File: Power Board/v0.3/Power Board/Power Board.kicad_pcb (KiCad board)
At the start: 2 copper layers, 66 x 80 mm, 72 parts, among them J1 Battery In, J2 JST B2PS-VH, J3 JST B2PS-VH, J4 JST B2PS-VH, J5 JST B2PS-VH, J6 JST B2PS-VH, J7 JST B2PS-VH, J8 Molex 70553-0006, Q1 SI5504BDC, SW1 SW_Push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

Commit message: Work in progress.
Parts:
- J1: footprint Power_Board:Molex_Microfit_43650-0203 -> Connector_JST:JST_VH_B3PS-VH_1x03_P3.96mm_Horizontal
- moved D1 32.0 mm to (124.0, 36.5)
- moved D2 32.0 mm to (130.2, 36.5)
- moved R1 32.0 mm to (124.0, 39.5)
- moved R2 32.0 mm to (130.1, 39.5)
- moved C5 27.0 mm to (99.0, 93.1)
- moved D3 27.0 mm to (94.0, 97.0)
- moved R5 27.0 mm to (97.0, 93.0)
- moved R6 27.0 mm to (97.0, 97.2)
- moved R7 27.0 mm to (99.0, 97.2)
- moved J1 21.6 mm to (105.0, 50.0), turned to 180 degrees
- moved C8 10.0 mm to (104.2, 80.0), turned to 180 degrees
- moved C10 9.19 mm to (107.2, 84.0)
- moved R12 9.06 mm to (100.0, 77.0)
- moved R8 9.06 mm to (100.0, 69.2)
- moved C2 9.00 mm to (99.8, 61.0)
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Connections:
- net Net-(C16-Pad1) renamed /Panel Power/Switch_Node
- net Net-(R18-Pad1) renamed /Panel Power/Drive_High_2
- net Net-(R18-Pad2) renamed /Panel Power/Drive_High_1
- net Net-(U2-Pad10) renamed /Panel Power/Drive_Low
- J1 pad 2: GND -> Net-(J1-Pad2)
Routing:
- net /5.2V_switched: track 0.00 -> 109.3 mm, vias 0 -> 2
- net /Pi Power/Power_Button: track 0.00 -> 72.0 mm
- net /Battery_Power: track 0.00 -> 69.8 mm
- net Net-(C5-Pad1): track 0.00 -> 39.6 mm, vias 0 -> 2
- net /Panel_Alert: track 0.00 -> 31.7 mm
- net /SCL: track 0.00 -> 23.7 mm
- net /Panel_Power: track 0.00 -> 21.5 mm, vias 0 -> 1
- net /SDA: track 0.00 -> 20.7 mm
- net Net-(C1-Pad1): track 0.00 -> 18.2 mm
- net /Panel Power/Vreg: track 0.00 -> 14.5 mm, vias 0 -> 2
- net Net-(C15-Pad1): track 0.00 -> 12.6 mm
- net Net-(C8-Pad2): track 0.00 -> 10.8 mm
- net Net-(R20-Pad2): track 0.00 -> 9.85 mm
- net Net-(R17-Pad2): track 0.00 -> 8.63 mm
- net Net-(R8-Pad2): track 0.00 -> 8.04 mm
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- added copper zone on F.Cu, net /5.2V_switched
- added copper zone on F.Cu, net /Battery_Power
- added copper zone on F.Cu, net /Panel Power/Switch_Node
- added copper zone on B.Cu, net /Panel_Power
- added copper zone on F.Cu, net /Panel_Power
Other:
- net class Panel_Battery added: clearance 0.1524, trace_width 3, via_dia 1, via_drill 0.5
- net class Panel_Drive added: clearance 0.1524, trace_width 0.25, via_dia 0.508, via_drill 0.254
- net class Pi_Battery added: clearance 0.1524, trace_width 0.3, via_dia 1.016, via_drill 0.508
- net class Pi_Power added: clearance 0.1524, trace_width 1.4, via_dia 0.508, via_drill 0.254

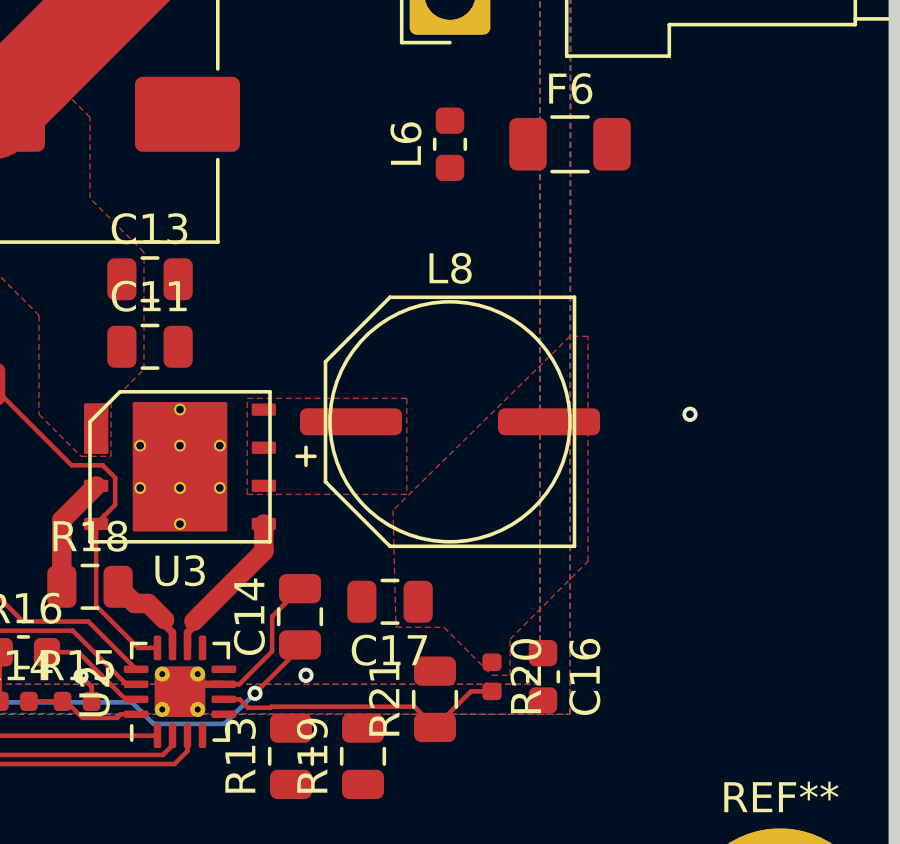
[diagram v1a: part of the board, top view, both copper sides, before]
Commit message: L8 footprint is Coilcraft XAL1580, not some Kemet cap.
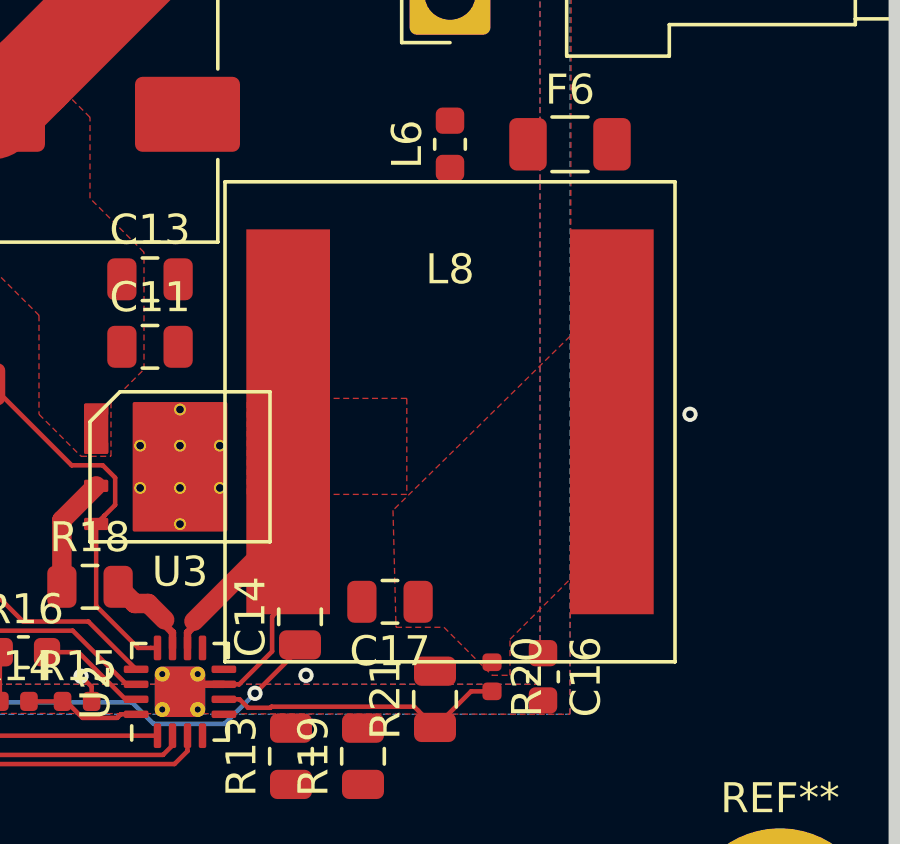
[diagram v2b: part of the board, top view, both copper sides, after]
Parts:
- L8: footprint Power_Board:CP_Kemet_8.3x10 -> Power_Board:Coilcraft_XAL1580
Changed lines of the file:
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@@
     (solder_mask_min_width 0.25)
     (aux_axis_origin 0 0)
-    (visible_elements FFFFFF7F)
+    (visible_elements FFFFEF7F)
     (pcbplotparams
       (layerselection 0x010fc_ffffffff)
@@
     (add_net /+5.2V)
   )
+  (module Power_Board:Coilcraft_XAL1580 (layer F.Cu)
+    (at 128 94.25 180)
+    (fp_text reference L8 (at 0 5.08 180) (layer F.SilkS)
+      (effects (font (size 1 1) (thickness 0.15)))
+    )
+    (fp_text value 1.3µH (at 0 -5.08 180) (layer F.Fab)
+      (effects (font (size 1 1) (thickness 0.15)))
+    )
+    (fp_line (start 7.75 8.25) (end 7.75 -8.25) (layer F.CrtYd) (width 0.12))
+    (fp_line (start -7.75 8.25) (end 7.75 8.25) (layer F.CrtYd) (width 0.12))
+    (fp_line (start -7.75 -8.25) (end -7.75 8.25) (layer F.CrtYd) (width 0.12))
+    (fp_line (start 7.75 -8.25) (end -7.75 -8.25) (layer F.CrtYd) (width 0.12))
+    (fp_line (start 7.5 8) (end 7.5 -8) (layer F.SilkS) (width 0.12))
+    (fp_line (start -7.5 8) (end 7.5 8) (layer F.SilkS) (width 0.12))
+    (fp_line (start -7.5 -8) (end -7.5 8) (layer F.SilkS) (width 0.12))
+    (fp_line (start 7.5 -8) (end -7.5 -8) (layer F.SilkS) (width 0.12))
+    (pad 2 smd rect (at -5.395 0 180) (size 2.79 12.83) (layers F.Cu F.Paste F.Mask)
+      (net 13 /Panel_Power))
+    (pad 1 smd rect (at 5.395 0 180) (size 2.79 12.83) (layers F.Cu F.Paste F.Mask)
+      (net 44 "/Panel Power/Switch_Node"))
+  )
   (module Power_Board:Q5D (layer F.Cu)
     (at 119 95.75)
@@
     (pad 1 thru_hole circle (at 0 0) (size 6.4 6.4) (drill 3.2) (layers *.Cu *.Mask))
   )
-  (module Power_Board:CP_Kemet_8.3x10 (layer F.Cu)
-    (at 128 94.25 180)
-    (fp_text reference L8 (at 0 5.08 180) (layer F.SilkS)
-      (effects (font (size 1 1) (thickness 0.15)))
-    )
-    (fp_text value 1.3µH (at 0 -5.08 180) (layer F.Fab)
-      (effects (font (size 1 1) (thickness 0.15)))
-    )
-    (fp_line (start 4.25 0.55) (end 4.25 2.05) (layer F.CrtYd) (width 0.12))
-    (fp_line (start 5.1 0.55) (end 4.25 0.55) (layer F.CrtYd) (width 0.12))
-    (fp_line (start 5.1 -0.55) (end 5.1 0.55) (layer F.CrtYd) (width 0.12))
-    (fp_line (start 4.25 -0.55) (end 5.1 -0.55) (layer F.CrtYd) (width 0.12))
-    (fp_line (start 4.25 -2) (end 4.25 -0.55) (layer F.CrtYd) (width 0.12))
-    (fp_line (start -4.3 -4.25) (end -4.25 -4.25) (layer F.CrtYd) (width 0.12))
-    (fp_line (start -4.3 -0.55) (end -4.3 -4.25) (layer F.CrtYd) (width 0.12))
-    (fp_line (start -5.1 -0.55) (end -4.3 -0.55) (layer F.CrtYd) (width 0.12))
-    (fp_line (start -5.1 0.55) (end -5.1 -0.55) (layer F.CrtYd) (width 0.12))
-    (fp_line (start -4.25 0.55) (end -5.1 0.55) (layer F.CrtYd) (width 0.12))
-    (fp_line (start -4.25 4.25) (end -4.25 0.55) (layer F.CrtYd) (width 0.12))
-    (fp_line (start 2.05 4.25) (end -4.25 4.25) (layer F.CrtYd) (width 0.12))
-    (fp_line (start 4.25 2.05) (end 2.05 4.25) (layer F.CrtYd) (width 0.12))
-    (fp_line (start 2 -4.25) (end 4.25 -2) (layer F.CrtYd) (width 0.12))
-    (fp_line (start -4.25 -4.25) (end 2 -4.25) (layer F.CrtYd) (width 0.12))
-    (fp_line (start 5.1 -1.15) (end 4.5 -1.15) (layer F.SilkS) (width 0.12))
-    (fp_line (start 4.8 -1.45) (end 4.8 -0.85) (layer F.SilkS) (width 0.12))
-    (fp_line (start -4.15 -4.15) (end -4.15 4.15) (layer F.SilkS) (width 0.12))
-    (fp_line (start 2 -4.15) (end -4.15 -4.15) (layer F.SilkS) (width 0.12))
-    (fp_line (start 4.15 -2) (end 2 -4.15) (layer F.SilkS) (width 0.12))
-    (fp_line (start 4.15 2) (end 4.15 -2) (layer F.SilkS) (width 0.12))
-    (fp_line (start 2 4.15) (end 4.15 2) (layer F.SilkS) (width 0.12))
-    (fp_line (start -4.15 4.15) (end 2 4.15) (layer F.SilkS) (width 0.12))
-    (fp_circle (center 0 0) (end 4 0) (layer F.SilkS) (width 0.12))
-    (pad 2 smd roundrect (at -3.3 0 180) (size 3.4 0.9) (layers F.Cu F.Paste F.Mask) (roundrect_rratio 0.25)
-      (net 13 /Panel_Power))
-    (pad 1 smd roundrect (at 3.3 0 180) (size 3.4 0.9) (layers F.Cu F.Paste F.Mask) (roundrect_rratio 0.25)
-      (net 44 "/Panel Power/Switch_Node"))
-  )
   (module Resistor_SMD:R_0805_2012Metric (layer F.Cu)
